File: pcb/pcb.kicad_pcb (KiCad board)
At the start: 4 copper layers, 56 x 40 mm, 93 parts, among them J1 Connector, J2 Tag connect TC2030-CTX, J3 USB C 2.0 Receptacle, SW1 RESET, U1 nRF52840, U2 USBLC6-2SC6, U3 LD39200PU33R, U4 nRF21540, U5 SX1262IMLTRT, U6 BGS12WN6E6327, Y1 32MHz, Y2 32.768kHz, Y3 KT2520K-T

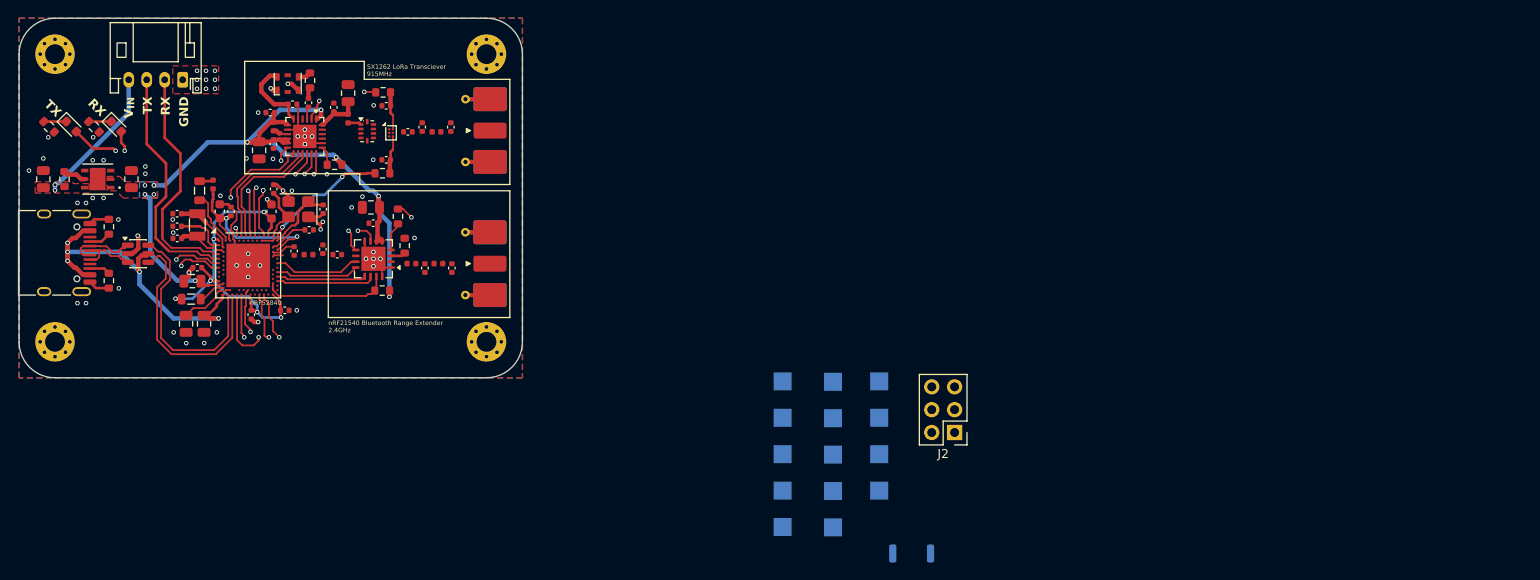
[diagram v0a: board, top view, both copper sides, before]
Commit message: switch TCXO, laid out from ref design from nordic
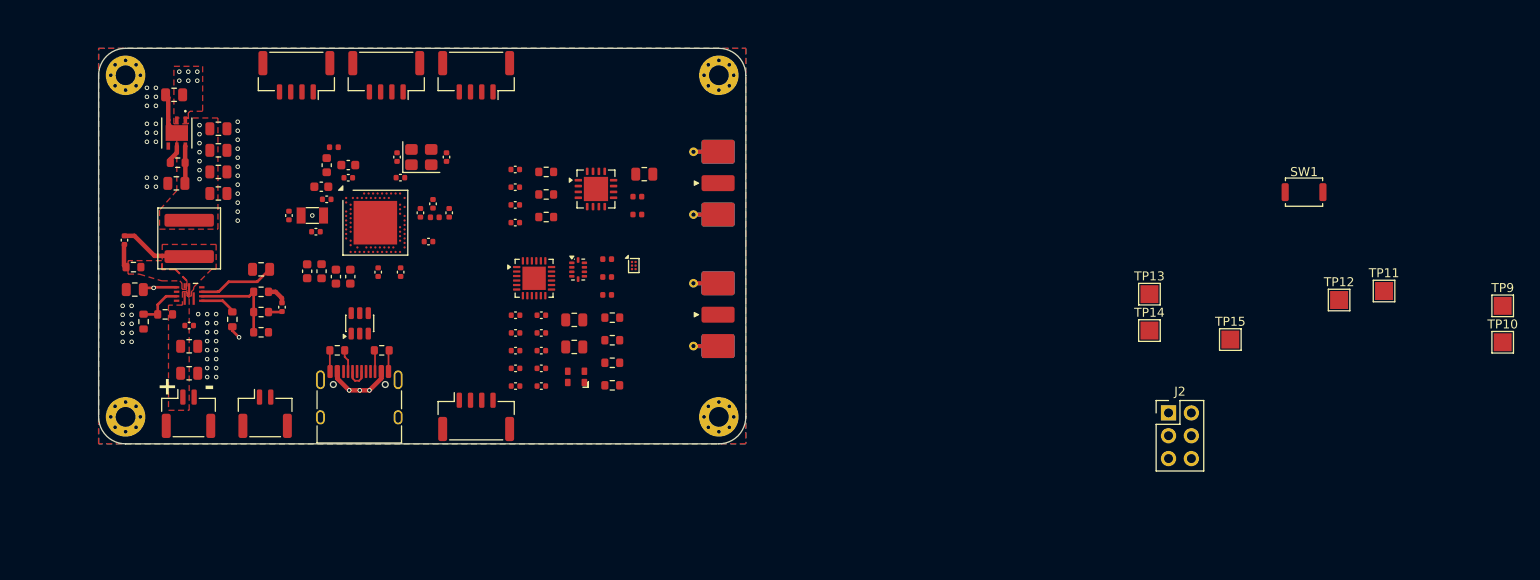
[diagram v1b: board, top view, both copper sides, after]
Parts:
- removed D1: RED, LED_SMD:LED_0603_1608Metric
- removed D2: YELLOW, LED_SMD:LED_0603_1608Metric
- removed TP1: LORA_SCK, TestPoint:TestPoint_Pad_2.0x2.0mm
- removed TP2: LORA_MOSI, TestPoint:TestPoint_Pad_2.0x2.0mm
- removed TP3: LORA_MISO, TestPoint:TestPoint_Pad_2.0x2.0mm
- removed TP4: LORA_CS, TestPoint:TestPoint_Pad_2.0x2.0mm
- removed TP5: BT_SCK, TestPoint:TestPoint_Pad_2.0x2.0mm
- removed TP6: BT_MOSI, TestPoint:TestPoint_Pad_2.0x2.0mm
- removed TP7: BT_MISO, TestPoint:TestPoint_Pad_2.0x2.0mm
- removed TP8: BT_CS, TestPoint:TestPoint_Pad_2.0x2.0mm
- removed Y3: KT2520K-T, Oscillator:Oscillator_SMD_Kyocera_2520-6Pin_2.5x2.0mm
- added C11: 820pF, Capacitor_SMD:C_0402_1005Metric, F.Cu at (137.6, 98.8)
- added C41: 10uF, Capacitor_SMD:C_0805_2012Metric, F.Cu at (110.9, 110.5)
- added C42: 10uF, Capacitor_SMD:C_0805_2012Metric, F.Cu at (110.9, 113.5)
- added C43: 100nF, Capacitor_SMD:C_0402_1005Metric, F.Cu at (110.9, 108.2)
- added C44: 100nF, Capacitor_SMD:C_0402_1005Metric, F.Cu at (103.7, 98.7)
- added C45: 22uF, Capacitor_SMD:C_0805_2012Metric, F.Cu at (114.2, 86.3)
- added C46: 22uF, Capacitor_SMD:C_0805_2012Metric, F.Cu at (114.2, 88.7)
- added C47: 22uF, Capacitor_SMD:C_0805_2012Metric, F.Cu at (114.2, 91.1)
- added C48: 22uF, Capacitor_SMD:C_0805_2012Metric, F.Cu at (114.2, 93.5)
- added C49: 1uF, Capacitor_SMD:C_0805_2012Metric, F.Cu at (104.9, 104.2)
- added C50: NC, Capacitor_SMD:C_0805_2012Metric, F.Cu at (118.9, 101.9)
- added C51: 22pF, Capacitor_SMD:C_0402_1005Metric, F.Cu at (121.2, 106.1)
- added J4: LoRa Test Conn, Connector_JST:JST_GH_SM04B-GHS-TB_1x04-1MP_P1.25mm_Horizontal, F.Cu at (142.8, 118.3)
- added J5: BT Test Conn, Connector_JST:JST_GH_SM04B-GHS-TB_1x04-1MP_P1.25mm_Horizontal, F.Cu at (142.8, 80.3)
- added J6: I2C 1, Connector_JST:JST_GH_SM04B-GHS-TB_1x04-1MP_P1.25mm_Horizontal, F.Cu at (132.8, 80.3)
- added J7: I2C 2, Connector_JST:JST_GH_SM04B-GHS-TB_1x04-1MP_P1.25mm_Horizontal, F.Cu at (122.8, 80.3)
- added J8: UART, Connector_JST:JST_GH_SM02B-GHS-TB_1x02-1MP_P1.25mm_Horizontal, F.Cu at (119.4, 118.0)
- added L10: 1.5uH, Inductor_SMD:L_Coilcraft_XAL6030-XXX, F.Cu at (110.9, 98.5)
- added R13: 0, Resistor_SMD:R_0603_1608Metric, F.Cu at (118.9, 106.7)
- added R14: 20k, Resistor_SMD:R_0603_1608Metric, F.Cu at (118.9, 108.9)
- added R15: 0, Resistor_SMD:R_0603_1608Metric, F.Cu at (104.7, 101.7)
- added R16: 20k, Resistor_SMD:R_0603_1608Metric, F.Cu at (108.2, 107.0)
- added R17: 20k, Resistor_SMD:R_0603_1608Metric, F.Cu at (105.8, 107.8)
- added TP15: V_{IN}, TestPoint:TestPoint_Pad_2.0x2.0mm, F.Cu at (226.8, 109.8)
- added U7: ECS-TXO-20CSMV4-320-AY-TR, footprints:Oscillator_SMD_ECS_2016, F.Cu at (153.4, 113.7)
- added U8: TPS51386RJNR, footprints:VQFN-HR12_RJN_TEX, F.Cu at (110.9, 104.7)
- C15, C16, C21: footprint Capacitor_SMD:C_0805_2012Metric -> Capacitor_SMD:C_0603_1608Metric
- J1: value Connector -> Battery; footprint Connector_JST:JST_PH_S4B-PH-K_1x04_P2.00mm_Horizontal -> Connector_JST:JST_GH_SM02B-GHS-TB_1x02-1MP_P1.25mm_Horizontal
- L2, L3: footprint Inductor_SMD:L_0805_2012Metric -> Inductor_SMD:L_0603_1608Metric
- R1: value 680 -> 100k
- R2: value 680 -> 150k
- SW1, TP10, TP11, TP12, TP14, TP9: moved to F.Cu
- TP13: value V_{IN} -> 5V; moved to F.Cu
- U3: footprint footprint-lib:SON_DFN6_3X3_STM -> footprints:SON_DFN6_3X3_STM
- moved H3 74.3 mm to (169.8, 118.3), turned to 90 degrees
- moved H4 73.9 mm to (169.8, 80.3), turned to 90 degrees
- moved TP9 72.3 mm to (257.1, 106.0), turned to 0 degrees
- moved TP10 70.5 mm to (257.1, 110.0), turned to 0 degrees
- moved TP11 68.4 mm to (243.8, 104.3), turned to 0 degrees
- moved SW1 59.3 mm to (234.9, 93.3), turned to 0 degrees
- moved TP12 52.0 mm to (238.8, 105.3), turned to 0 degrees
- moved R10 44.3 mm to (158.0, 109.8), turned to 0 degrees
- moved R12 41.4 mm to (158.0, 114.8)
- moved TP14 41.2 mm to (217.8, 108.8), turned to 0 degrees
- moved H1 41.0 mm to (103.8, 118.3), turned to 90 degrees
- moved H2 40.2 mm to (103.8, 80.3), turned to 90 degrees
- moved L7 39.9 mm to (157.4, 100.8), turned to 0 degrees
- moved C31 39.8 mm to (153.8, 107.6), turned to 0 degrees
- moved C34 39.4 mm to (147.2, 113.0), turned to 0 degrees
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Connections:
- C22 pad 1: V_{IN} -> +5V
- J1 pad 1: GND -> V_{IN}
- J1 pad 2: UART_RX -> GND
- R1 pad 2: GND -> Net-(U8-PG)
- R2 pad 2: GND -> +5V
- R5 pad 1: V_{IN} -> +5V
- TP13 pad 1: V_{IN} -> +5V
- U3 pad 6: V_{IN} -> +5V
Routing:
- net +3.3V: track 88.6 -> 0.00 mm, vias 10 -> 6
- net BT_MODE: track 42.5 -> 0.00 mm, vias 2 -> 0
- net /MCU/VDD: track 40.4 -> 0.00 mm, vias 6 -> 0
- net GND: track 47.9 -> 9.52 mm, vias 67 -> 56
- net BT_RX_EN: track 32.3 -> 0.00 mm, vias 2 -> 0
- net LORA_CS: track 31.5 -> 0.00 mm, vias 2 -> 0
- net VBUS: track 38.9 -> 7.54 mm, vias 5 -> 3
- net BT_TX_EN: track 30.6 -> 0.00 mm, vias 2 -> 0
- net UART_TX: track 27.0 -> 0.00 mm
- net UART_RX: track 26.3 -> 0.00 mm
- net USB_D+: track 26.2 -> 0.00 mm
- net /MCU/TX_LED: track 25.5 -> 0.00 mm, vias 2 -> 0
- net USB_D-: track 25.5 -> 0.00 mm
- net /MCU/RX_LED: track 23.1 -> 0.00 mm, vias 2 -> 0
- net /MCU/DCC: track 21.6 -> 0.00 mm, vias 2 -> 0
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- added copper zone on F.Cu, net +5V
- added copper zone on F.Cu, net Net-(U8-SW)
- added copper zone on F.Cu, net Net-(U8-VBST)
- removed copper zone on B.Cu, net +3.3V
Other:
- board size 56 x 40 mm -> 72 x 44 mm
- board text added: "+"
- board text added: "-"
- board text removed: "GND"
- board text removed: "RX"
- board text removed: "SX1262 LoRa Transciever 915MHz"
- board text removed: "TX"
- board text removed: "V_{IN}"
- board text removed: "nRF21540 Bluetooth Range Extender 2.4GHz"
- board text removed: "nRF52840"

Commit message: V2
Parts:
- removed the J2 at (219.9, 117.9)
- added C19: DNP, Capacitor_SMD:C_0402_1005Metric, F.Cu at (137.9, 94.2)
- added R18: 5.1k, Resistor_SMD:R_0603_1608Metric, F.Cu at (120.5, 87.1)
- added R19: 5.1k, Resistor_SMD:R_0603_1608Metric, F.Cu at (123.6, 87.1)
- added R20: 5.1k, Resistor_SMD:R_0603_1608Metric, F.Cu at (134.4, 86.0)
- added R21: 5.1k, Resistor_SMD:R_0603_1608Metric, F.Cu at (131.2, 86.0)
- added TP10: TestPoint, TestPoint:TestPoint_Pad_D1.0mm, B.Cu at (135.6, 104.1)
- added TP11: TestPoint, TestPoint:TestPoint_Pad_D1.0mm, B.Cu at (137.6, 106.1)
- added TP8: TestPoint, TestPoint:TestPoint_Pad_D1.0mm, B.Cu at (135.6, 106.1)
- added TP9: TestPoint, TestPoint:TestPoint_Pad_D1.0mm, B.Cu at (137.6, 104.1)
- C36: renamed from C26; footprint Capacitor_SMD:C_0805_2012Metric -> Capacitor_SMD:C_0603_1608Metric
- C40: renamed from C31; footprint Capacitor_SMD:C_0805_2012Metric -> Capacitor_SMD:C_0603_1608Metric
- C45: renamed from C33; footprint Capacitor_SMD:C_0805_2012Metric -> Capacitor_SMD:C_0603_1608Metric
- J3: renamed from J6; value I2C 1 -> I2C 2
- J6: renamed from J7; value I2C 2 -> I2C 1
- TP1: renamed from TP9; footprint TestPoint:TestPoint_Pad_2.0x2.0mm -> TestPoint:TestPoint_Pad_D1.0mm; moved to B.Cu
- TP2: renamed from TP10; footprint TestPoint:TestPoint_Pad_2.0x2.0mm -> TestPoint:TestPoint_Pad_D1.0mm; moved to B.Cu
- TP3: renamed from TP12; footprint TestPoint:TestPoint_Pad_2.0x2.0mm -> TestPoint:TestPoint_Pad_D1.0mm; moved to B.Cu
- TP4: renamed from TP11; footprint TestPoint:TestPoint_Pad_2.0x2.0mm -> TestPoint:TestPoint_Pad_D1.0mm; moved to B.Cu
- TP5: renamed from TP15; footprint TestPoint:TestPoint_Pad_2.0x2.0mm -> TestPoint:TestPoint_Pad_D1.0mm; moved to B.Cu
- TP6: renamed from TP13; footprint TestPoint:TestPoint_Pad_2.0x2.0mm -> TestPoint:TestPoint_Pad_D1.0mm; moved to B.Cu
- TP7: renamed from TP14; footprint TestPoint:TestPoint_Pad_2.0x2.0mm -> TestPoint:TestPoint_Pad_D1.0mm; moved to B.Cu
- moved TP2 139.3 mm to (117.8, 114.4), turned to 180 degrees
- moved TP1 136.5 mm to (120.8, 114.4), turned to 180 degrees
- moved TP5 118.2 mm to (108.8, 116.4), turned to 180 degrees
- moved SW1 111.0 mm to (124.9, 107.3), turned to -90 degrees
- moved TP4 110.6 mm to (133.3, 105.9), turned to 180 degrees
- moved TP7 108.0 mm to (112.8, 83.4), turned to 180 degrees
- moved TP6 106.6 mm to (112.8, 86.4), turned to 180 degrees
- moved TP3 104.2 mm to (134.7, 101.0), turned to 180 degrees
- moved L8 21.3 mm to (137.8, 108.9), turned to -90 degrees
- moved C40 17.8 mm to (136.4, 111.3), turned to -90 degrees
- moved R15 17.3 mm to (141.8, 103.7), turned to -90 degrees
- moved C36 16.2 mm to (145.3, 91.0), turned to 180 degrees
- moved U6 16.1 mm to (139.9, 105.0), turned to 180 degrees
- moved R16 14.2 mm to (144.8, 112.5), turned to 90 degrees
- moved L9 12.6 mm to (146.0, 108.1), turned to -90 degrees
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- renumbered C6 to C1, C17 to C11, C10 to C12, C21 to C13, C11 to C14, C18 to C15, C12 to C16, C19 to C17, C13 to C18, C7 to C2, C15 to C21, C44 to C22, C41 to C23, C42 to C24, C43 to C25, C45 to C26, C46 to C27, C47 to C28, C48 to C29, C51 to C30, C50 to C31, C49 to C32, C23 to C33, C22 to C34, C25 to C35, C27 to C37, C28 to C38, C24 to C39, C2 to C4, C32 to C41, C34 to C42, C36 to C43, C29 to C44, C35 to C46, C30 to C47, C38 to C48, C39 to C49, C40 to C50, C37 to C51, C3 to C6, C4 to C7, C16 to C9, J8 to J2, J3 to J8, L2 to L1, L9 to L10, L4 to L2, L1 to L4, L10 to L5, L5 to L6, L6 to L7, L7 to L8, L8 to L9, R3 to R1, R5 to R10, R7 to R11, R6 to R12, R8 to R13, R11 to R14, R10 to R15, R9 to R16, R12 to R17, R4 to R2, R15 to R3, R16 to R4, R17 to R5, R2 to R6, R1 to R7, R13 to R8, R14 to R9, U8 to U3, U3 to U4, U4 to U5, U7 to U6, U5 to U7, U6 to U8, Y2 to Y1, Y1 to Y2
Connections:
- net nRF_TRX renamed BT_TRX
- J3 pad 2: /I2C1_SCL -> I2C2_SCL
- J3 pad 3: /I2C1_SDA -> I2C2_SDA
- J4 pad 1: /LORA_CS -> LORA_CS
- J4 pad 2: /LORA_MISO -> LORA_MISO
- J4 pad 3: /LORA_MOSI -> LORA_MOSI
- J4 pad 4: /LORA_SCK -> LORA_SCK
- J5 pad 1: /BT_CS -> BT_CS
- J5 pad 2: /BT_MISO -> BT_MISO
- J5 pad 3: /BT_MOSI -> BT_MOSI
- J5 pad 4: /BT_SCK -> BT_SCK
- J6 pad 2: /I2C2_SCL -> I2C1_SCL
- J6 pad 3: /I2C2_SDA -> I2C1_SDA
- U1 pad A10: LORA_BUSY -> BT_RX_EN
- U1 pad A12: LORA_NRST -> BT_TX_EN
- U1 pad A14: LORA_MISO -> I2C1_SCL
- U1 pad A16: LORA_MOSI -> I2C2_SDA
- U1 pad A20: LORA_SCK -> I2C2_SCL
- U1 pad AD10: LORA_CS -> LORA_MISO
- U1 pad AD18: BT_RX_EN -> LORA_MOSI
- U1 pad AD20: BT_TX_EN -> LORA_SCK
- U1 pad AD8: BT_MODE -> LORA_CS
- U1 pad B19: ANT_SW -> unconnected-(U1-P1.11-PadB19)
- U1 pad G1: UART_RX -> I2C1_SDA
- U1 pad J1: UART_TX -> LORA_NRST
- U1 pad J24: unconnected-(U1-NFC2/P0.10-PadJ24) -> BT_PDN
- U1 pad L1: /MCU/TX_LED -> BT_MODE
- U1 pad L24: BT_PDN -> LORA_BUSY
- U1 pad N1: /MCU/RX_LED -> ANT_SW
- U1 pad R1: unconnected-(U1-TRACEDATA3/P1.09-PadR1) -> UART_RX
- U1 pad U1: unconnected-(U1-TRACEDATA1/P0.12-PadU1) -> UART_TX
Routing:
- net +3.3V: track 0.00 -> 164.0 mm, vias 6 -> 16
- net ANT_SW: track 0.00 -> 59.5 mm, vias 0 -> 2
- net LORA_CS: track 0.00 -> 59.3 mm, vias 0 -> 2
- net +5V: track 6.70 -> 63.4 mm, vias 7 -> 10
- net GND: track 9.52 -> 63.4 mm, vias 56 -> 134
- net BT_MODE: track 0.00 -> 52.4 mm, vias 0 -> 2
- net /MCU/VDD: track 0.00 -> 49.0 mm, vias 0 -> 6
- net DIO1: track 0.00 -> 41.1 mm, vias 0 -> 2
- net LORA_MISO: track 0.00 -> 40.9 mm, vias 0 -> 2
- net BT_CS: track 0.00 -> 40.1 mm, vias 0 -> 2
- net LORA_SCK: track 0.00 -> 35.4 mm, vias 0 -> 2
- net BT_MISO: track 0.00 -> 33.5 mm, vias 0 -> 2
- net LORA_NRST: track 0.00 -> 31.8 mm, vias 0 -> 2
- net BT_MOSI: track 0.00 -> 29.8 mm, vias 0 -> 2
- net BT_SCK: track 0.00 -> 29.5 mm, vias 0 -> 2
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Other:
- board size 72 x 44 mm -> 65 x 44 mm
- board text added: "3.3V"
- board text added: "5V"
- board text added: "5V SDA SCL GND"
- board text added: "BOOT"
- board text added: "BT"
- board text added: "CLK"
- board text added: "CS MISO MOSI SCK"
- board text added: "DIO"
- board text added: "I^{2}C1"
- board text added: "I^{2}C2"
- board text added: "LoRa"
- board text added: "RESET"
- board text added: "RST"
- board text added: "RX"
- board text added: "RX TX"
- board text added: "SCK MOSI MISO CS"
- board text added: "SWO"
- board text added: "TX"
- board text added: "UART"
- board text added: "VDD"
- board text added: "V_{IN}"
- board text removed: "-"

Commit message: V2 fixup
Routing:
- net UART_RX: track 26.7 -> 27.5 mm
- net UART_TX: track 25.5 -> 26.3 mm

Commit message: fix SWD position
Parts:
- added TP12: TestPoint, TestPoint:TestPoint_Pad_D1.0mm, B.Cu at (135.6, 104.1)
- moved TP10 2.83 mm to (137.6, 102.1)
- moved TP3 1.39 mm to (135.6, 102.1)
- moved TP4 0.23 mm to (133.4, 106.1)
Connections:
- net BT_TRX renamed nRF_TRX
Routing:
- net /MCU/SWDIO: track 6.62 -> 3.96 mm, vias 2 -> 1
- net /MCU/VDD: track 49.0 -> 50.5 mm
- net GND: track 63.4 -> 64.6 mm, vias 134 -> 138
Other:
- board text added: "Designed by Dylan DiBeneditto"
- board text added: "GND"
- board text added: "LoRa (915MHz) and Bluetooth (2.4GHz) transciever"
- board text added: "NRST"
- board text added: "SWD"
- board text removed: "RST"

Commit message: revision 3
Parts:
- removed C19: DNP, Capacitor_SMD:C_0402_1005Metric
- removed J2: UART, Connector_JST:JST_GH_SM02B-GHS-TB_1x02-1MP_P1.25mm_Horizontal
- removed L3: 10uH, Inductor_SMD:L_0603_1608Metric
- removed TP1: UART_TX, TestPoint:TestPoint_Pad_D1.0mm
- removed TP10, TP11, TP12, TP9: TestPoint, TestPoint:TestPoint_Pad_D1.0mm
- removed TP2: UART_RX, TestPoint:TestPoint_Pad_D1.0mm
- removed TP3: VDD (nRF regulated), TestPoint:TestPoint_Pad_D1.0mm
- added D1: Red, LED_SMD:LED_0603_1608Metric, F.Cu at (115.2, 83.2)
- added D2: DSS110U, Diode_SMD:D_SOD-123F, F.Cu at (109.8, 93.5)
- added D3: DSS110U, Diode_SMD:D_SOD-123F, F.Cu at (105.2, 93.5)
- added J7: SWD Breakout, Connector_PinHeader_2.54mm:PinHeader_2x03_P2.54mm_Vertical, F.Cu at (140.3, 81.7)
- added J9: UART, Connector_JST:JST_GH_SM04B-GHS-TB_1x04-1MP_P1.25mm_Horizontal, F.Cu at (119.4, 118.0)
- J4: value LoRa Test Conn -> LoRa Debug; footprint Connector_JST:JST_GH_SM04B-GHS-TB_1x04-1MP_P1.25mm_Horizontal -> Connector_PinHeader_2.54mm:PinHeader_2x03_P2.54mm_Vertical
- J5: value BT Test Conn -> BT Debug; footprint Connector_JST:JST_GH_SM04B-GHS-TB_1x04-1MP_P1.25mm_Horizontal -> Connector_PinHeader_2.54mm:PinHeader_2x02_P2.54mm_Vertical
- R3: value 0 -> 680
- R4, R5: value 20k -> 100k
- TP4: moved to F.Cu
- TP8: value TestPoint -> DCC
- moved SW1 41.9 mm to (156.9, 80.3), turned to 180 degrees
- moved R3 22.8 mm to (115.2, 81.5), turned to 0 degrees
- moved TP8 12.8 mm to (138.8, 93.7)
- moved TP6 9.24 mm to (106.0, 92.6)
- moved TP4 8.83 mm to (124.5, 105.8), turned to 0 degrees
- moved J4 7.39 mm to (148.6, 119.6), turned to 90 degrees
- moved J5 6.29 mm to (149.0, 79.1), turned to 0 degrees
- moved TP7 4.12 mm to (116.8, 84.0)
- moved C9 1.88 mm to (125.7, 102.7)
- moved C34 1.08 mm to (109.4, 91.3)
- moved U4 0.90 mm to (109.5, 85.9)
- moved R10 0.90 mm to (109.6, 89.2)
- moved C43 0.60 mm to (152.6, 112.1)
- moved R14 0.60 mm to (151.2, 113.5)
- moved C33 0.10 mm to (109.2, 82.4)
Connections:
- C11 pad 1: /MCU/VDD -> +3.3V
- C15 pad 1: /MCU/VDD -> +3.3V
- C17 pad 1: /MCU/VDD -> +3.3V
- C20 pad 1: /MCU/VDD -> +3.3V
- C22 pad 1: Net-(C22-Pad1) -> Net-(U3-VBST)
- C34 pad 1: +5V -> Net-(D2-K)
- J4 pad 1: LORA_CS -> LORA_SCK
- J4 pad 2: LORA_MISO -> LORA_CS
- J4 pad 4: LORA_SCK -> LORA_BUSY
- J5 pad 1: BT_CS -> BT_SCK
- J5 pad 4: BT_SCK -> BT_CS
- R10 pad 1: +5V -> Net-(D2-K)
- R3 pad 1: Net-(U3-VBST) -> Net-(D1-K)
- R3 pad 2: Net-(C22-Pad1) -> GND
- TP6 pad 1: +5V -> Net-(D2-K)
- TP8 pad 1: /MCU/SWO -> /MCU/DCC
- U1 pad A22: /MCU/VDD -> +3.3V
- U1 pad AB2: Net-(U1-DCCH) -> unconnected-(U1-DCCH-PadAB2)
- U1 pad AD14: /MCU/VDD -> +3.3V
- U1 pad AD23: /MCU/VDD -> +3.3V
- U1 pad B1: /MCU/VDD -> +3.3V
- U1 pad W1: /MCU/VDD -> +3.3V
- U4 pad 6: +5V -> Net-(D2-K)
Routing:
- net /MCU/VDD: track 50.5 -> 0.00 mm, vias 6 -> 0
- net VBUS: track 32.2 -> 81.2 mm, vias 5 -> 7
- net +3.3V: track 164.0 -> 206.0 mm, vias 16 -> 22
- net /MCU/SWO: track 7.05 -> 33.4 mm, vias 1 -> 2
- net /MCU/NRST: track 24.1 -> 49.1 mm, vias 2 -> 4
- net /MCU/SWDIO: track 3.96 -> 26.9 mm, vias 1 -> 3
- net /MCU/SWDCLK: track 7.56 -> 30.2 mm, vias 1 -> 2
- net DIO1: track 41.1 -> 57.4 mm
- net LORA_MISO: track 40.9 -> 55.4 mm
- net LORA_BUSY: track 29.0 -> 42.3 mm
- net +5V: track 63.4 -> 74.1 mm, vias 10 -> 11
- net Net-(U3-VBST): track 0.00 -> 10.2 mm
- net LORA_MOSI: track 27.2 -> 36.9 mm
- net /MCU/BOOT/DFU: track 6.49 -> 15.4 mm, vias 1 -> 2
- net BT_SCK: track 29.5 -> 35.9 mm, vias 2 -> 1
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- added copper zone on F.Cu, net Net-(D2-K)
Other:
- board text added: "5V RX TX GND"
- board text added: "BT SPI"
- board text added: "BUSY"
- board text added: "CS"
- board text added: "DCC"
- board text added: "DIO1"
- board text added: "LoRa SPI"
- board text added: "MISO"
- board text added: "MOSI"
- board text added: "SCK"
- board text removed: "BT"
- board text removed: "CS MISO MOSI SCK"
- board text removed: "LoRa"
- board text removed: "RX"
- board text removed: "RX TX"
- board text removed: "SCK MOSI MISO CS"
- board text removed: "TX"
- board text removed: "VDD"

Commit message: update readme
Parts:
- added G***: LOGO, LOGO, B.Cu at (121.7, 95.8)
- moved TP4 0.30 mm to (124.8, 105.8)
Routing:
- net GND: track 63.9 -> 69.2 mm
- net +3.3V: track 206.0 -> 209.3 mm
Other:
- board text added: "Rocketry @ VT"
